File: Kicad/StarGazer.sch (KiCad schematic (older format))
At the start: 5 parts, among them U101 STM32F070F6Px

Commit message: Continued (slow) devolopment.
PCB board has begun.  Parts are pushed out to where they need to roughly be.
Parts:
- removed C101, C102: 4.7uF, Capacitor_SMD:C_0805_2012Metric_Pad1.15x1.40mm_HandSolder, symbol Device:C_Small
- removed R101, R102: 10k, Resistor_SMD:R_1206_3216Metric_Pad1.42x1.75mm_HandSolder, symbol Device:R
- removed U101: STM32F070F6Px, Package_SO:TSSOP-20_4.4x6.5mm_P0.65mm, symbol MCU_ST_STM32F0:STM32F070F6Px
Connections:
- net labels removed: GND, I2C_SCL, I2C_SDA, OSC_IN, OSC_OUT, RESET_N, SHIFT_REG_CLK, SHIFT_REG_DATA_IN, SHIFT_REG_LATCH, SHIFT_REG_RESET_N, SWCLK, SWDIO, UI_BUTTON, UI_JOY_X, UI_JOY_Y, V_REG
- wire segments 34 -> 0
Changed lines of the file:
@@
 $Descr A4 11693 8268
 encoding utf-8
-Sheet 1 3
+Sheet 1 1
 Title ""
 Date ""
@@
 Comment4 ""
 $EndDescr
-Wire Wire Line
-	4800 4075 4375 4075
-Wire Wire Line
-	4800 4175 4375 4175
-Text GLabel 4375 4075 0    50   BiDi ~ 0
-OSC_IN
-Text GLabel 4375 4175 0    50   BiDi ~ 0
-OSC_OUT
-$Comp
-L power:GND #PWR0103
-U 1 1 5F3EE3F5
-P 5300 4850
-F 0 "#PWR0103" H 5300 4600 50  0001 C CNN
-F 1 "GND" H 5305 4677 50  0000 C CNN
-F 2 "" H 5300 4850 50  0001 C CNN
-F 3 "" H 5300 4850 50  0001 C CNN
-	1    5300 4850
-	1    0    0    -1
-$EndComp
-Wire Wire Line
-	5300 4575 5300 4850
-Wire Wire Line
-	6100 3975 6200 3975
-Text GLabel 6200 4275 2    50   BiDi ~ 0
-SWDIO
-Text GLabel 6200 4375 2    50   BiDi ~ 0
-SWCLK
-Wire Wire Line
-	6100 4375 6200 4375
-Wire Wire Line
-	6100 4275 6200 4275
-Text GLabel 6200 4175 2    50   BiDi ~ 0
-I2C_SDA
-Text GLabel 6200 4075 2    50   BiDi ~ 0
-I2C_SCL
-Wire Wire Line
-	6100 4175 6200 4175
-Wire Wire Line
-	6100 4075 6200 4075
-Wire Wire Line
-	4800 3275 4375 3275
-Text GLabel 4375 3275 0    50   BiDi ~ 0
-RESET_N
-$Comp
-L MCU_ST_STM32F0:STM32F070F6Px U101
-U 1 1 5F3ECB3C
-P 5500 3775
-F 0 "U101" H 5450 2886 50  0000 C CNN
-F 1 "STM32F070F6Px" H 5450 2795 50  0000 C CNN
-F 2 "Package_SO:TSSOP-20_4.4x6.5mm_P0.65mm" H 4900 3075 50  0001 R CNN
-F 3 "http://www.st.com/st-web-ui/static/active/en/resource/technical/document/datasheet/DM00141386.pdf" H 5500 3775 50  0001 C CNN
-F 4 "Cortex M0 48MHz" H 5500 3775 50  0001 C CNN "part_details"
-F 5 "STM32F070F6P6TR" H 5500 3775 50  0001 C CNN "part_name"
-F 6 "https://www.digikey.com/product-detail/en/stmicroelectronics/STM32F070F6P6TR/497-17354-1-ND/8024125" H 5500 3775 50  0001 C CNN "part_url"
-	1    5500 3775
-	1    0    0    -1
-$EndComp
-Wire Wire Line
-	4650 3475 4800 3475
-$Comp
-L Device:R R101
-U 1 1 5F3FCFD6
-P 4500 3475
-F 0 "R101" V 4293 3475 50  0000 C CNN
-F 1 "10k" V 4384 3475 50  0000 C CNN
-F 2 "Resistor_SMD:R_1206_3216Metric_Pad1.42x1.75mm_HandSolder" V 4430 3475 50  0001 C CNN
-F 3 "~" H 4500 3475 50  0001 C CNN
-F 4 "" H 4500 3475 50  0001 C CNN "Name"
-F 5 "" H 4500 3475 50  0001 C CNN "part_details"
-F 6 "Resistor - Pull Up" H 4500 3475 50  0001 C CNN "part_name"
-F 7 "https://www.digikey.com/product-detail/en/yageo/RC1206JR-0710KL/311-10KERCT-ND/732156" H 4500 3475 50  0001 C CNN "part_url"
-	1    4500 3475
-	0    -1   -1   0
-$EndComp
-Wire Wire Line
-	4175 3475 4350 3475
-Wire Wire Line
-	4175 3475 4175 3550
-$Comp
-L power:GND #PWR0101
-U 1 1 5F3FD5C8
-P 4175 3550
-F 0 "#PWR0101" H 4175 3300 50  0001 C CNN
-F 1 "GND" H 4180 3377 50  0000 C CNN
-F 2 "" H 4175 3550 50  0001 C CNN
-F 3 "" H 4175 3550 50  0001 C CNN
-	1    4175 3550
-	1    0    0    -1
-$EndComp
-Text GLabel 5300 2175 0    51   BiDi ~ 0
-V_REG
-$Comp
-L Device:C_Small C101
-U 1 1 5F4EAC14
-P 5000 2500
-F 0 "C101" V 4771 2500 50  0000 C CNN
-F 1 "4.7uF" V 4862 2500 50  0000 C CNN
-F 2 "Capacitor_SMD:C_0805_2012Metric_Pad1.15x1.40mm_HandSolder" H 5000 2500 50  0001 C CNN
-F 3 "~" H 5000 2500 50  0001 C CNN
-F 4 "" V 5000 2500 50  0001 C CNN "TestField"
-F 5 "https://www.digikey.com/product-detail/en/w%C3%BCrth-elektronik/885012107009/732-7619-1-ND/5454246" H 5000 2500 50  0001 C CNN "part_url"
-F 6 "Capactitor - Bypass" H 5000 2500 50  0001 C CNN "part_name"
-	1    5000 2500
-	0    1    1    0
-$EndComp
-$Comp
-L Device:C_Small C102
-U 1 1 5F4EB59B
-P 5000 2850
-F 0 "C102" V 4771 2850 50  0000 C CNN
-F 1 "4.7uF" V 4862 2850 50  0000 C CNN
-F 2 "Capacitor_SMD:C_0805_2012Metric_Pad1.15x1.40mm_HandSolder" H 5000 2850 50  0001 C CNN
-F 3 "~" H 5000 2850 50  0001 C CNN
-F 4 "https://www.digikey.com/product-detail/en/w%C3%BCrth-elektronik/885012107009/732-7619-1-ND/5454246" H 5000 2850 50  0001 C CNN "part_url"
-F 5 "Capactitor - Bypass" H 5000 2850 50  0001 C CNN "part_name"
-	1    5000 2850
-	0    1    1    0
-$EndComp
-Wire Wire Line
-	5300 2175 5300 2500
-Wire Wire Line
-	5100 2850 5300 2850
-Connection ~ 5300 2850
-Wire Wire Line
-	5100 2500 5300 2500
-Connection ~ 5300 2500
-Wire Wire Line
-	5300 2500 5300 2850
-Wire Wire Line
-	4900 2500 4775 2500
-Wire Wire Line
-	4775 2500 4775 2850
-Wire Wire Line
-	4900 2850 4775 2850
-Connection ~ 4775 2850
-Wire Wire Line
-	4775 2850 4775 2950
-$Comp
-L power:GND #PWR0102
-U 1 1 5F4F9B1C
-P 4775 2950
-F 0 "#PWR0102" H 4775 2700 50  0001 C CNN
-F 1 "GND" H 4780 2777 50  0000 C CNN
-F 2 "" H 4775 2950 50  0001 C CNN
-F 3 "" H 4775 2950 50  0001 C CNN
-	1    4775 2950
-	1    0    0    -1
-$EndComp
-Wire Wire Line
-	5300 2850 5300 3075
-Wire Wire Line
-	5300 2850 5400 2850
-Wire Wire Line
-	5400 2850 5400 3075
-Wire Wire Line
-	6100 3575 6175 3575
-Text GLabel 6175 3575 2    50   BiDi ~ 0
-SHIFT_REG_LATCH
-$Comp
-L power:GND #PWR0104
-U 1 1 5F5511AD
-P 7350 3975
-F 0 "#PWR0104" H 7350 3725 50  0001 C CNN
-F 1 "GND" H 7355 3802 50  0000 C CNN
-F 2 "" H 7350 3975 50  0001 C CNN
-F 3 "" H 7350 3975 50  0001 C CNN
-	1    7350 3975
-	1    0    0    -1
-$EndComp
-Wire Wire Line
-	7350 3975 7350 3875
-Wire Wire Line
-	6100 3775 6200 3775
-Text GLabel 6200 3775 2    50   BiDi ~ 0
-SHIFT_REG_CLK
-Text GLabel 6200 3975 2    50   BiDi ~ 0
-SHIFT_REG_DATA_IN
-Wire Wire Line
-	7350 3675 7225 3675
-Wire Wire Line
-	6925 3675 6100 3675
-$Comp
-L Device:R R102
-U 1 1 5F54B516
-P 7075 3675
-F 0 "R102" V 6868 3675 50  0000 C CNN
-F 1 "10k" V 6959 3675 50  0000 C CNN
-F 2 "Resistor_SMD:R_1206_3216Metric_Pad1.42x1.75mm_HandSolder" V 7005 3675 50  0001 C CNN
-F 3 "~" H 7075 3675 50  0001 C CNN
-F 4 "" H 7075 3675 50  0001 C CNN "Name"
-F 5 "" H 7075 3675 50  0001 C CNN "part_details"
-F 6 "Resistor - Pull Up" H 7075 3675 50  0001 C CNN "part_name"
-F 7 "https://www.digikey.com/product-detail/en/yageo/RC1206JR-0710KL/311-10KERCT-ND/732156" H 7075 3675 50  0001 C CNN "part_url"
-	1    7075 3675
-	0    1    1    0
-$EndComp
-Wire Wire Line
-	6100 3375 6175 3375
-Text GLabel 4375 4375 0    47   BiDi ~ 0
-UI_BUTTON
-Text GLabel 6175 3375 2    47   BiDi ~ 0
-UI_JOY_X
-Text GLabel 6175 3475 2    47   BiDi ~ 0
-UI_JOY_Y
-Wire Wire Line
-	4375 4375 4800 4375
-Wire Wire Line
-	6100 3475 6175 3475
-$Sheet
-S -13400 250  10700 7900
-U 5F580D08
-F0 "Schematic_Test_Power" 50
-F1 "Schematic_Test_Power.sch" 50
-$EndSheet
-$Sheet
-S 12400 -100 10850 9900
-U 5F580392
-F0 "Schematic_Test_Digital" 50
-F1 "Schematic_Test_Digital.sch" 50
-$EndSheet
-Text GLabel 6175 3275 2    50   BiDi ~ 0
-SHIFT_REG_RESET_N
-Wire Wire Line
-	6100 3275 6175 3275
-Wire Wire Line
-	6100 3875 7350 3875
-Connection ~ 7350 3875
-Wire Wire Line
-	7350 3875 7350 3675
 $EndSCHEMATC

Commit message: "PREVIOUS COMMIT MAIN SCHEMATIC CORRUPTED (???).  Used commit before that."
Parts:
- added C101, C102: 4.7uF, Capacitor_SMD:C_0805_2012Metric_Pad1.15x1.40mm_HandSolder, symbol Device:C_Small
- added R101, R102: 10k, Resistor_SMD:R_1206_3216Metric_Pad1.42x1.75mm_HandSolder, symbol Device:R
- added U101: STM32F070F6Px, Package_SO:TSSOP-20_4.4x6.5mm_P0.65mm, symbol MCU_ST_STM32F0:STM32F070F6Px
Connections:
- net labels added: GND, I2C_SCL, I2C_SDA, OSC_IN, OSC_OUT, RESET_N, SHIFT_REG_CLK, SHIFT_REG_DATA_IN, SHIFT_REG_LATCH, SHIFT_REG_RESET_N, SWCLK, SWDIO, UI_BUTTON, UI_JOY_X, UI_JOY_Y, V_REG
- wire segments 0 -> 34
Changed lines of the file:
@@
 $Descr A4 11693 8268
 encoding utf-8
-Sheet 1 1
+Sheet 1 3
 Title ""
 Date ""
@@
 Comment4 ""
 $EndDescr
+Wire Wire Line
+	4800 4075 4375 4075
+Wire Wire Line
+	4800 4175 4375 4175
+Text GLabel 4375 4075 0    50   BiDi ~ 0
+OSC_IN
+Text GLabel 4375 4175 0    50   BiDi ~ 0
+OSC_OUT
+$Comp
+L power:GND #PWR0103
+U 1 1 5F3EE3F5
+P 5300 4850
+F 0 "#PWR0103" H 5300 4600 50  0001 C CNN
+F 1 "GND" H 5305 4677 50  0000 C CNN
+F 2 "" H 5300 4850 50  0001 C CNN
+F 3 "" H 5300 4850 50  0001 C CNN
+	1    5300 4850
+	1    0    0    -1
+$EndComp
+Wire Wire Line
+	5300 4575 5300 4850
+Wire Wire Line
+	6100 3975 6200 3975
+Text GLabel 6200 4275 2    50   BiDi ~ 0
+SWDIO
+Text GLabel 6200 4375 2    50   BiDi ~ 0
+SWCLK
+Wire Wire Line
+	6100 4375 6200 4375
+Wire Wire Line
+	6100 4275 6200 4275
+Text GLabel 6200 4175 2    50   BiDi ~ 0
+I2C_SDA
+Text GLabel 6200 4075 2    50   BiDi ~ 0
+I2C_SCL
+Wire Wire Line
+	6100 4175 6200 4175
+Wire Wire Line
+	6100 4075 6200 4075
+Wire Wire Line
+	4800 3275 4375 3275
+Text GLabel 4375 3275 0    50   BiDi ~ 0
+RESET_N
+$Comp
+L MCU_ST_STM32F0:STM32F070F6Px U101
+U 1 1 5F3ECB3C
+P 5500 3775
+F 0 "U101" H 5450 2886 50  0000 C CNN
+F 1 "STM32F070F6Px" H 5450 2795 50  0000 C CNN
+F 2 "Package_SO:TSSOP-20_4.4x6.5mm_P0.65mm" H 4900 3075 50  0001 R CNN
+F 3 "http://www.st.com/st-web-ui/static/active/en/resource/technical/document/datasheet/DM00141386.pdf" H 5500 3775 50  0001 C CNN
+F 4 "Cortex M0 48MHz" H 5500 3775 50  0001 C CNN "part_details"
+F 5 "STM32F070F6P6TR" H 5500 3775 50  0001 C CNN "part_name"
+F 6 "https://www.digikey.com/product-detail/en/stmicroelectronics/STM32F070F6P6TR/497-17354-1-ND/8024125" H 5500 3775 50  0001 C CNN "part_url"
+	1    5500 3775
+	1    0    0    -1
+$EndComp
+Wire Wire Line
+	4650 3475 4800 3475
+$Comp
+L Device:R R101
+U 1 1 5F3FCFD6
+P 4500 3475
+F 0 "R101" V 4293 3475 50  0000 C CNN
+F 1 "10k" V 4384 3475 50  0000 C CNN
+F 2 "Resistor_SMD:R_1206_3216Metric_Pad1.42x1.75mm_HandSolder" V 4430 3475 50  0001 C CNN
+F 3 "~" H 4500 3475 50  0001 C CNN
+F 4 "" H 4500 3475 50  0001 C CNN "Name"
+F 5 "" H 4500 3475 50  0001 C CNN "part_details"
+F 6 "Resistor - Pull Up" H 4500 3475 50  0001 C CNN "part_name"
+F 7 "https://www.digikey.com/product-detail/en/yageo/RC1206JR-0710KL/311-10KERCT-ND/732156" H 4500 3475 50  0001 C CNN "part_url"
+	1    4500 3475
+	0    -1   -1   0
+$EndComp
+Wire Wire Line
+	4175 3475 4350 3475
+Wire Wire Line
+	4175 3475 4175 3550
+$Comp
+L power:GND #PWR0101
+U 1 1 5F3FD5C8
+P 4175 3550
+F 0 "#PWR0101" H 4175 3300 50  0001 C CNN
+F 1 "GND" H 4180 3377 50  0000 C CNN
+F 2 "" H 4175 3550 50  0001 C CNN
+F 3 "" H 4175 3550 50  0001 C CNN
+	1    4175 3550
+	1    0    0    -1
+$EndComp
+Text GLabel 5300 2175 0    51   BiDi ~ 0
+V_REG
+$Comp
+L Device:C_Small C101
+U 1 1 5F4EAC14
+P 5000 2500
+F 0 "C101" V 4771 2500 50  0000 C CNN
+F 1 "4.7uF" V 4862 2500 50  0000 C CNN
+F 2 "Capacitor_SMD:C_0805_2012Metric_Pad1.15x1.40mm_HandSolder" H 5000 2500 50  0001 C CNN
+F 3 "~" H 5000 2500 50  0001 C CNN
+F 4 "" V 5000 2500 50  0001 C CNN "TestField"
+F 5 "https://www.digikey.com/product-detail/en/w%C3%BCrth-elektronik/885012107009/732-7619-1-ND/5454246" H 5000 2500 50  0001 C CNN "part_url"
+F 6 "Capactitor - Bypass" H 5000 2500 50  0001 C CNN "part_name"
+	1    5000 2500
+	0    1    1    0
+$EndComp
+$Comp
+L Device:C_Small C102
+U 1 1 5F4EB59B
+P 5000 2850
+F 0 "C102" V 4771 2850 50  0000 C CNN
+F 1 "4.7uF" V 4862 2850 50  0000 C CNN
+F 2 "Capacitor_SMD:C_0805_2012Metric_Pad1.15x1.40mm_HandSolder" H 5000 2850 50  0001 C CNN
+F 3 "~" H 5000 2850 50  0001 C CNN
+F 4 "https://www.digikey.com/product-detail/en/w%C3%BCrth-elektronik/885012107009/732-7619-1-ND/5454246" H 5000 2850 50  0001 C CNN "part_url"
+F 5 "Capactitor - Bypass" H 5000 2850 50  0001 C CNN "part_name"
+	1    5000 2850
+	0    1    1    0
+$EndComp
+Wire Wire Line
+	5300 2175 5300 2500
+Wire Wire Line
+	5100 2850 5300 2850
+Connection ~ 5300 2850
+Wire Wire Line
+	5100 2500 5300 2500
+Connection ~ 5300 2500
+Wire Wire Line
+	5300 2500 5300 2850
+Wire Wire Line
+	4900 2500 4775 2500
+Wire Wire Line
+	4775 2500 4775 2850
+Wire Wire Line
+	4900 2850 4775 2850
+Connection ~ 4775 2850
+Wire Wire Line
+	4775 2850 4775 2950
+$Comp
+L power:GND #PWR0102
+U 1 1 5F4F9B1C
+P 4775 2950
+F 0 "#PWR0102" H 4775 2700 50  0001 C CNN
+F 1 "GND" H 4780 2777 50  0000 C CNN
+F 2 "" H 4775 2950 50  0001 C CNN
+F 3 "" H 4775 2950 50  0001 C CNN
+	1    4775 2950
+	1    0    0    -1
+$EndComp
+Wire Wire Line
+	5300 2850 5300 3075
+Wire Wire Line
+	5300 2850 5400 2850
+Wire Wire Line
+	5400 2850 5400 3075
+Wire Wire Line
+	6100 3575 6175 3575
+Text GLabel 6175 3575 2    50   BiDi ~ 0
+SHIFT_REG_LATCH
+$Comp
+L power:GND #PWR0104
+U 1 1 5F5511AD
+P 7350 3975
+F 0 "#PWR0104" H 7350 3725 50  0001 C CNN
+F 1 "GND" H 7355 3802 50  0000 C CNN
+F 2 "" H 7350 3975 50  0001 C CNN
+F 3 "" H 7350 3975 50  0001 C CNN
+	1    7350 3975
+	1    0    0    -1
+$EndComp
+Wire Wire Line
+	7350 3975 7350 3875
+Wire Wire Line
+	6100 3775 6200 3775
+Text GLabel 6200 3775 2    50   BiDi ~ 0
+SHIFT_REG_CLK
+Text GLabel 6200 3975 2    50   BiDi ~ 0
+SHIFT_REG_DATA_IN
+Wire Wire Line
+	7350 3675 7225 3675
+Wire Wire Line
+	6925 3675 6100 3675
+$Comp
+L Device:R R102
+U 1 1 5F54B516
+P 7075 3675
+F 0 "R102" V 6868 3675 50  0000 C CNN
+F 1 "10k" V 6959 3675 50  0000 C CNN
+F 2 "Resistor_SMD:R_1206_3216Metric_Pad1.42x1.75mm_HandSolder" V 7005 3675 50  0001 C CNN
+F 3 "~" H 7075 3675 50  0001 C CNN
+F 4 "" H 7075 3675 50  0001 C CNN "Name"
+F 5 "" H 7075 3675 50  0001 C CNN "part_details"
+F 6 "Resistor - Pull Up" H 7075 3675 50  0001 C CNN "part_name"
+F 7 "https://www.digikey.com/product-detail/en/yageo/RC1206JR-0710KL/311-10KERCT-ND/732156" H 7075 3675 50  0001 C CNN "part_url"
+	1    7075 3675
+	0    1    1    0
+$EndComp
+Wire Wire Line
+	6100 3375 6175 3375
+Text GLabel 4375 4375 0    47   BiDi ~ 0
+UI_BUTTON
+Text GLabel 6175 3375 2    47   BiDi ~ 0
+UI_JOY_X
+Text GLabel 6175 3475 2    47   BiDi ~ 0
+UI_JOY_Y
+Wire Wire Line
+	4375 4375 4800 4375
+Wire Wire Line
+	6100 3475 6175 3475
+$Sheet
+S -13400 250  10700 7900
+U 5F580D08
+F0 "Schematic_Test_Power" 50
+F1 "Schematic_Test_Power.sch" 50
+$EndSheet
+$Sheet
+S 12400 -100 10850 9900
+U 5F580392
+F0 "Schematic_Test_Digital" 50
+F1 "Schematic_Test_Digital.sch" 50
+$EndSheet
+Text GLabel 6175 3275 2    50   BiDi ~ 0
+SHIFT_REG_RESET_N
+Wire Wire Line
+	6100 3275 6175 3275
+Wire Wire Line
+	6100 3875 7350 3875
+Connection ~ 7350 3875
+Wire Wire Line
+	7350 3875 7350 3675
 $EndSCHEMATC

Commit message: Center LED ring laid out and connected. Other components will begin to be fitted into place. Silk screen has not been touched.
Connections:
- net labels added: SHIFT_REG_OUTPUT_ENABLE_N
- net labels removed: SHIFT_REG_RESET_N
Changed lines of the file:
@@
 Text GLabel 4375 4375 0    47   BiDi ~ 0
 UI_BUTTON
+Text GLabel 6175 3275 2    47   BiDi ~ 0
+UI_JOY_X
 Text GLabel 6175 3375 2    47   BiDi ~ 0
-UI_JOY_X
-Text GLabel 6175 3475 2    47   BiDi ~ 0
 UI_JOY_Y
 Wire Wire Line
@@
 F1 "Schematic_Test_Digital.sch" 50
 $EndSheet
-Text GLabel 6175 3275 2    50   BiDi ~ 0
-SHIFT_REG_RESET_N
+Text GLabel 6175 3475 2    50   BiDi ~ 0
+SHIFT_REG_OUTPUT_ENABLE_N
 Wire Wire Line
 	6100 3275 6175 3275

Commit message: Calculating ram needed and current selected chip will not fit it.  Upgrading to a more capable chip.
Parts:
- R101, R102: value 10k -> 10kohm
- U101: value STM32F070F6Px -> STM32F070F6P6TR; part_name STM32F070F6P6TR -> Cortex M0 Microcontroller
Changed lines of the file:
@@
 P 5500 3775
 F 0 "U101" H 5450 2886 50  0000 C CNN
-F 1 "STM32F070F6Px" H 5450 2795 50  0000 C CNN
+F 1 "STM32F070F6P6TR" H 5450 2795 50  0000 C CNN
 F 2 "Package_SO:TSSOP-20_4.4x6.5mm_P0.65mm" H 4900 3075 50  0001 R CNN
 F 3 "http://www.st.com/st-web-ui/static/active/en/resource/technical/document/datasheet/DM00141386.pdf" H 5500 3775 50  0001 C CNN
 F 4 "Cortex M0 48MHz" H 5500 3775 50  0001 C CNN "part_details"
-F 5 "STM32F070F6P6TR" H 5500 3775 50  0001 C CNN "part_name"
+F 5 "Cortex M0 Microcontroller" H 5500 3775 50  0001 C CNN "part_name"
 F 6 "https://www.digikey.com/product-detail/en/stmicroelectronics/STM32F070F6P6TR/497-17354-1-ND/8024125" H 5500 3775 50  0001 C CNN "part_url"
 	1    5500 3775
@@
 P 4500 3475
 F 0 "R101" V 4293 3475 50  0000 C CNN
-F 1 "10k" V 4384 3475 50  0000 C CNN
+F 1 "10kohm" V 4384 3475 50  0000 C CNN
 F 2 "Resistor_SMD:R_1206_3216Metric_Pad1.42x1.75mm_HandSolder" V 4430 3475 50  0001 C CNN
 F 3 "~" H 4500 3475 50  0001 C CNN
@@
 P 7075 3675
 F 0 "R102" V 6868 3675 50  0000 C CNN
-F 1 "10k" V 6959 3675 50  0000 C CNN
+F 1 "10kohm" V 6959 3675 50  0000 C CNN
 F 2 "Resistor_SMD:R_1206_3216Metric_Pad1.42x1.75mm_HandSolder" V 7005 3675 50  0001 C CNN
 F 3 "~" H 7075 3675 50  0001 C CNN

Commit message: Upgraded to STM32G0 for increased memory. Schematic and PCB are updated.  PCB now has radial grid applied in preparation of final part placement.
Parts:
- removed R102: 10kohm, Resistor_SMD:R_1206_3216Metric_Pad1.42x1.75mm_HandSolder, symbol Device:R
- removed U101: STM32F070F6P6TR, Package_SO:TSSOP-20_4.4x6.5mm_P0.65mm, symbol MCU_ST_STM32F0:STM32F070F6Px
- added D101: Green, Diode_SMD:D_1206_3216Metric, symbol Device:LED
- added D102: Red, Diode_SMD:D_1206_3216Metric, symbol Device:LED
- added R102, R103: 180ohm, Resistor_SMD:R_1206_3216Metric_Pad1.42x1.75mm_HandSolder, symbol Device:R_Small
- added TP101, TP102: Connector_TestPoint, TestPoint:TestPoint_Pad_D1.0mm, symbol StarGazer-cache:Connector_TestPoint
- added U101: STM32G070KBT6, Package_QFP:LQFP-32_7x7mm_P0.8mm, symbol StarGazer:STM32G070KBT6
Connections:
- wire segments 34 -> 44
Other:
- note added: "STM32G070KB\nFLASH : 128Kb\nSRAM : 32KB\n64MHz (max)\n2.0v - 3.6v\n\nAll unused GPIO should be set as output through programming.\n\nSPI1_NSS (slave select) can be set as GPIO if unused.\nSPI1_MISO (master in) can be set as GPIO if unused."
- moved on the sheet: C101, C102, R101

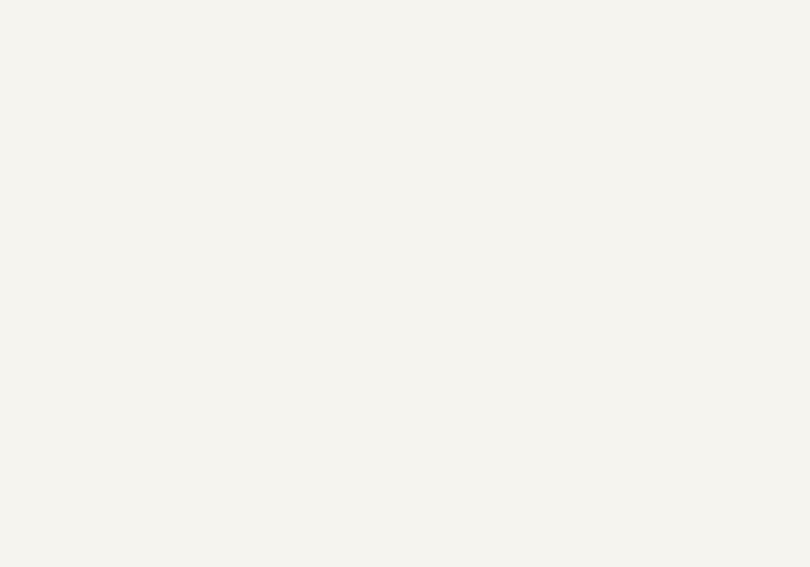
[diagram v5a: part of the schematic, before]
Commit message: Shift register tracing remade to curved.  Hand hurty
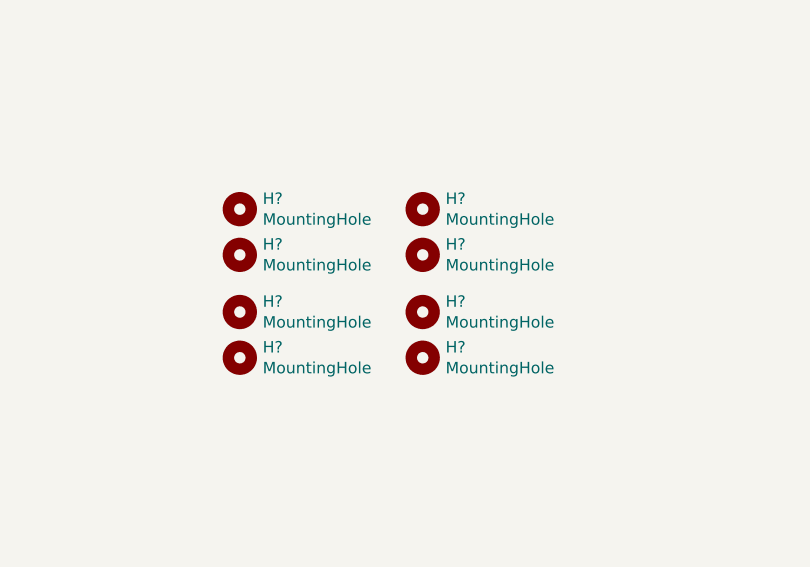
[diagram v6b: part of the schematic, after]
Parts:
- added H? (x8): MountingHole, MountingHole:MountingHole_2.2mm_M2, symbol Mechanical:MountingHole
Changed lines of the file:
@@
+	1    0    0    -1
+$EndComp
+$Comp
+L Mechanical:MountingHole H?
+U 1 1 5F61C377
+P 5600 7200
+F 0 "H?" H 5700 7246 50  0000 L CNN
+F 1 "MountingHole" H 5700 7155 50  0000 L CNN
+F 2 "MountingHole:MountingHole_2.2mm_M2" H 5600 7200 50  0001 C CNN
+F 3 "~" H 5600 7200 50  0001 C CNN
+F 4 "DO_NOT_SHOW" H 5600 7200 50  0001 C CNN "part_details"
+	1    5600 7200
+	1    0    0    -1
+$EndComp
+$Comp
+L Mechanical:MountingHole H?
+U 1 1 5F61C9F3
+P 5600 7400
+F 0 "H?" H 5700 7446 50  0000 L CNN
+F 1 "MountingHole" H 5700 7355 50  0000 L CNN
+F 2 "MountingHole:MountingHole_2.2mm_M2" H 5600 7400 50  0001 C CNN
+F 3 "~" H 5600 7400 50  0001 C CNN
+F 4 "DO_NOT_SHOW" H 5600 7400 50  0001 C CNN "part_details"
+	1    5600 7400
+	1    0    0    -1
+$EndComp
+$Comp
+L Mechanical:MountingHole H?
+U 1 1 5F61EB9F
+P 5600 6750
+F 0 "H?" H 5700 6796 50  0000 L CNN
+F 1 "MountingHole" H 5700 6705 50  0000 L CNN
+F 2 "MountingHole:MountingHole_2.2mm_M2" H 5600 6750 50  0001 C CNN
+F 3 "~" H 5600 6750 50  0001 C CNN
+F 4 "DO_NOT_SHOW" H 5600 6750 50  0001 C CNN "part_details"
+	1    5600 6750
+	1    0    0    -1
+$EndComp
+$Comp
+L Mechanical:MountingHole H?
+U 1 1 5F61EBA6
+P 5600 6950
+F 0 "H?" H 5700 6996 50  0000 L CNN
+F 1 "MountingHole" H 5700 6905 50  0000 L CNN
+F 2 "MountingHole:MountingHole_2.2mm_M2" H 5600 6950 50  0001 C CNN
+F 3 "~" H 5600 6950 50  0001 C CNN
+F 4 "DO_NOT_SHOW" H 5600 6950 50  0001 C CNN "part_details"
+	1    5600 6950
+	1    0    0    -1
+$EndComp
+$Comp
+L Mechanical:MountingHole H?
+U 1 1 5F61FCE3
+P 4800 7200
+F 0 "H?" H 4900 7246 50  0000 L CNN
+F 1 "MountingHole" H 4900 7155 50  0000 L CNN
+F 2 "MountingHole:MountingHole_2.2mm_M2" H 4800 7200 50  0001 C CNN
+F 3 "~" H 4800 7200 50  0001 C CNN
+F 4 "DO_NOT_SHOW" H 4800 7200 50  0001 C CNN "part_details"
+	1    4800 7200
+	1    0    0    -1
+$EndComp
+$Comp
+L Mechanical:MountingHole H?
+U 1 1 5F61FCEA
+P 4800 7400
+F 0 "H?" H 4900 7446 50  0000 L CNN
+F 1 "MountingHole" H 4900 7355 50  0000 L CNN
+F 2 "MountingHole:MountingHole_2.2mm_M2" H 4800 7400 50  0001 C CNN
+F 3 "~" H 4800 7400 50  0001 C CNN
+F 4 "DO_NOT_SHOW" H 4800 7400 50  0001 C CNN "part_details"
+	1    4800 7400
+	1    0    0    -1
+$EndComp
+$Comp
+L Mechanical:MountingHole H?
+U 1 1 5F61FCF1
+P 4800 6750
+F 0 "H?" H 4900 6796 50  0000 L CNN
+F 1 "MountingHole" H 4900 6705 50  0000 L CNN
+F 2 "MountingHole:MountingHole_2.2mm_M2" H 4800 6750 50  0001 C CNN
+F 3 "~" H 4800 6750 50  0001 C CNN
+F 4 "DO_NOT_SHOW" H 4800 6750 50  0001 C CNN "part_details"
+	1    4800 6750
+	1    0    0    -1
+$EndComp
+$Comp
+L Mechanical:MountingHole H?
+U 1 1 5F61FCF8
+P 4800 6950
+F 0 "H?" H 4900 6996 50  0000 L CNN
+F 1 "MountingHole" H 4900 6905 50  0000 L CNN
+F 2 "MountingHole:MountingHole_2.2mm_M2" H 4800 6950 50  0001 C CNN
+F 3 "~" H 4800 6950 50  0001 C CNN
+F 4 "DO_NOT_SHOW" H 4800 6950 50  0001 C CNN "part_details"
+	1    4800 6950
 	1    0    0    -1
 $EndComp
